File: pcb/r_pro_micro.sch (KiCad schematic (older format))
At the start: 27 parts, among them J1 Conn_01x12, J2 USB_A, J3 Conn_01x12, U1 MIC5219-2.5YM5, U2 ATmega32U4-MU, Y1 16MHz

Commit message: ** e agrega informacion de digikey en componentes importantes **
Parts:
- D1: DK# (none) -> B0520WS-FDITR-ND; MFG# (none) -> B0520WS-7-F; Manufacturer (none) -> Diodes Incorporated
- F1: DK# (none) -> 507-1762-2-ND; MFG# (none) -> 0ZCG0050AF2C; Manufacturer (none) -> Bel Fuse Inc.
- J1, J3: DK# (none) -> S1032E-12-ND; MFG# (none) -> PEC12SACN; Manufacturer (none) -> Sullins Connector Solutions
- J2: DK# (none) -> WM17143TR-ND; MFG# (none) -> 0475890001; Manufacturer (none) -> Molex
- U1: DK# (none) -> MIC5219-2.85BMM-TR-ND; MFG# (none) -> MIC5219-2.85BMM-TR; Manufacturer (none) -> Microchip Technology
- U2: DK# (none) -> ATMEGA32U4-MU-ND; MFG# (none) -> ATMEGA32U4-MU; Manufacturer (none) -> Microchip Technology
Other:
- note removed: "Digikey N producto: 507-1762-2-ND\nNumero pieza fabricante: 0ZCG0050AF2C\nDescripcion: PTC RESET FUSE 30V 500MA 1812\nProovedor: Bel Fuse Inc."
- note removed: "Digikey N producto: ATMEGA32U4-MU-ND\nDescripcion: IC MCU 8BIT 32KB FLASH 44VQFN\nProovedor: Microchip Technology"
- note removed: "Digikey N producto: B0520WS-FDITR-ND\nDescripcion: DIODE SCHOTTKY 20V 500MA SOD323\nProovedor: Diodes Incorporated"
- note removed: "Digikey N producto: MIC5219-2.85BMM-ND\nDescripcion: IC REG LINEAR 2.85V 500MA 8MSOP\nProovedor: Microchip Technology"
- note removed: "Digikey N producto: S1032E-12-ND\nDescripcion: CONN HEADER VERT 12POS 2.54MM\nProovedor: Sullins Connector Solutions"
- note removed: "Digikey N producto: WM17143TR-ND\nNumero pieza fabricante: 0475890001\nDescripcion: CONN RCPT MICRO USB AB 5P SMD RA\nProovedor: Molex"
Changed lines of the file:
@@
 F 2 "Connector_PinHeader_2.54mm:PinHeader_1x12_P2.54mm_Vertical" H 10650 3200 50  0001 C CNN
 F 3 "~" H 10650 3200 50  0001 C CNN
+F 4 "PEC12SACN" H 10650 3200 50  0001 C CNN "MFG#"
+F 5 "S1032E-12-ND" H 10650 3200 50  0001 C CNN "DK#"
+F 6 "Sullins Connector Solutions" H 10650 3200 50  0001 C CNN "Manufacturer"
 	1    10650 3200
 	1    0    0    -1
@@
 F 2 "Connector_USB:USB_Micro-AB_Molex_47590-0001" H 3200 4350 50  0001 C CNN
 F 3 " ~" H 3200 4350 50  0001 C CNN
+F 4 "0475890001" H 3050 4400 50  0001 C CNN "MFG#"
+F 5 "WM17143TR-ND" H 3050 4400 50  0001 C CNN "DK#"
+F 6 "Molex" H 3050 4400 50  0001 C CNN "Manufacturer"
 	1    3050 4400
 	1    0    0    -1
@@
 F 2 "Connector_PinHeader_2.54mm:PinHeader_1x12_P2.54mm_Vertical" H 8950 3300 50  0001 C CNN
 F 3 "~" H 8950 3300 50  0001 C CNN
+F 4 "PEC12SACN" H 8950 3300 50  0001 C CNN "MFG#"
+F 5 "S1032E-12-ND" H 8950 3300 50  0001 C CNN "DK#"
+F 6 "Sullins Connector Solutions" H 8950 3300 50  0001 C CNN "Manufacturer"
 	1    8950 3300
 	-1   0    0    1
@@
 F 2 "Package_DFN_QFN:QFN-44-1EP_7x7mm_P0.5mm_EP5.2x5.2mm" H 6400 3750 50  0001 C CIN
 F 3 "http://ww1.microchip.com/downloads/en/DeviceDoc/Atmel-7766-8-bit-AVR-ATmega16U4-32U4_Datasheet.pdf" H 6400 3750 50  0001 C CNN
+F 4 "ATMEGA32U4-MU" H 6400 3750 50  0001 C CNN "MFG#"
+F 5 "ATMEGA32U4-MU-ND" H 6400 3750 50  0001 C CNN "DK#"
+F 6 "Microchip Technology" H 6400 3750 50  0001 C CNN "Manufacturer"
 	1    6400 3750
 	1    0    0    -1
@@
 Wire Wire Line
 	5150 3350 5800 3350
-Wire Notes Line
-	6800 5450 7050 5700
-Wire Notes Line
-	7050 5700 7600 5700
-Text Notes 7050 5700 0    50   ~ 0
-Digikey N producto: ATMEGA32U4-MU-ND\nDescripcion: IC MCU 8BIT 32KB FLASH 44VQFN\nProovedor: Microchip Technology
-Text Notes 9300 4350 0    50   ~ 0
-Digikey N producto: S1032E-12-ND\nDescripcion: CONN HEADER VERT 12POS 2.54MM\nProovedor: Sullins Connector Solutions
-Wire Notes Line
-	9000 3850 9300 4100
-Wire Notes Line
-	9300 4100 9850 4100
-Wire Notes Line
-	700  1350 1350 1350
-Text Notes 2750 1650 0    50   ~ 0
-Digikey N producto: MIC5219-2.85BMM-ND\nDescripcion: IC REG LINEAR 2.85V 500MA 8MSOP\nProovedor: Microchip Technology
-Wire Notes Line
-	700  2900 1200 2900
-Wire Notes Line
-	950  1800 700  2900
-Wire Notes Line
-	2750 1650 3100 1650
-Wire Notes Line
-	2500 1900 2750 1650
 $Comp
 L Device:C_Small C6
@@
 F 2 "Diode_SMD:D_SOD-323" V 1450 1750 50  0001 C CNN
 F 3 "~" V 1450 1750 50  0001 C CNN
+F 4 "B0520WS-7-F" H 1450 1750 50  0001 C CNN "MFG#"
+F 5 "B0520WS-FDITR-ND" H 1450 1750 50  0001 C CNN "DK#"
+F 6 "Diodes Incorporated" H 1450 1750 50  0001 C CNN "Manufacturer"
 	1    1450 1750
 	-1   0    0    1
@@
 F 2 "Fuse:Fuse_1206_3216Metric" H 1050 1550 50  0001 L CNN
 F 3 "~" H 1000 1750 50  0001 C CNN
+F 4 "0ZCG0050AF2C" V 1000 1750 50  0001 C CNN "MFG#"
+F 5 "507-1762-2-ND" V 1000 1750 50  0001 C CNN "DK#"
+F 6 "Bel Fuse Inc." V 1000 1750 50  0001 C CNN "Manufacturer"
 	1    1000 1750
 	0    1    1    0
@@
 F 2 "Package_TO_SOT_SMD:SOT-23-5" H 2350 2525 50  0001 C CNN
 F 3 "http://ww1.microchip.com/downloads/en/DeviceDoc/MIC5219-500mA-Peak-Output-LDO-Regulator-DS20006021A.pdf" H 2350 2200 50  0001 C CNN
+F 4 "MIC5219-2.85BMM-TR" H 2350 2200 50  0001 C CNN "MFG#"
+F 5 "MIC5219-2.85BMM-TR-ND" H 2350 2200 50  0001 C CNN "DK#"
+F 6 "Microchip Technology" H 2350 2200 50  0001 C CNN "Manufacturer"
 	1    2350 2200
 	1    0    0    -1
 $EndComp
-Wire Notes Line
-	1400 1700 700  1350
-Text Notes 700  3250 0    50   ~ 0
-Digikey N producto: 507-1762-2-ND\nNumero pieza fabricante: 0ZCG0050AF2C\nDescripcion: PTC RESET FUSE 30V 500MA 1812\nProovedor: Bel Fuse Inc.
-Text Notes 700  1350 0    50   ~ 0
-Digikey N producto: B0520WS-FDITR-ND\nDescripcion: DIODE SCHOTTKY 20V 500MA SOD323\nProovedor: Diodes Incorporated
-Wire Notes Line
-	2850 4700 2300 5400
-Wire Notes Line
-	2300 5400 2900 5400
-Text Notes 2300 5750 0    50   ~ 0
-Digikey N producto: WM17143TR-ND\nNumero pieza fabricante: 0475890001\nDescripcion: CONN RCPT MICRO USB AB 5P SMD RA\nProovedor: Molex
 Text Label 9400 2800 0    50   ~ 0
 RXI

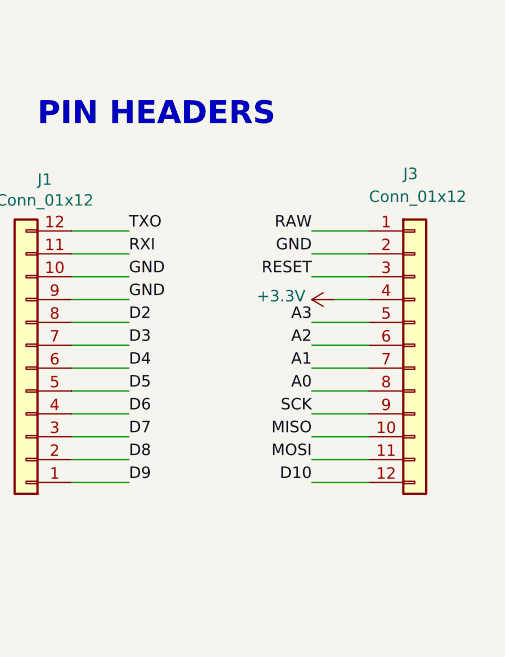
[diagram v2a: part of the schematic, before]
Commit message: ** Se rehace posicionamiento de footprints **
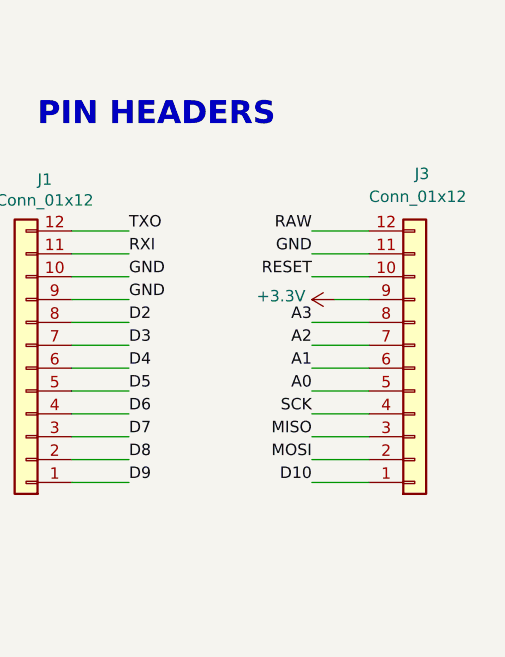
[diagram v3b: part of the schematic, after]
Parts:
- D1: footprint Diode_SMD:D_SOD-323 -> Diode_SMD:D_SOD-523
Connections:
- net +3V3: now also J3.9 (Pin_9); no longer J3.4 (Pin_4)
- net A0: now also J3.5 (Pin_5); no longer J3.8 (Pin_8)
- net A1: now also J3.6 (Pin_6); no longer J3.7 (Pin_7)
- net A2: now also J3.7 (Pin_7); no longer J3.6 (Pin_6)
- net A3: now also J3.8 (Pin_8); no longer J3.5 (Pin_5)
- net D10: now also J3.1 (Pin_1); no longer J3.12 (Pin_12)
- net GND: now also J3.11 (Pin_11); no longer J3.2 (Pin_2)
- net MISO: now also J3.3 (Pin_3); no longer J3.10 (Pin_10)
- net MOSI: now also J3.2 (Pin_2); no longer J3.11 (Pin_11)
- net RAW: now also J3.12 (Pin_12); no longer J3.1 (Pin_1)
- net RESET: now also J3.10 (Pin_10); no longer J3.3 (Pin_3)
- net SCK: now also J3.4 (Pin_4); no longer J3.9 (Pin_9)
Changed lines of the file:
@@
 L Connector_Generic:Conn_01x12 J3
 U 1 1 5F5DDF99
-P 10650 3200
-F 0 "J3" H 10600 3950 50  0000 L CNN
-F 1 "Conn_01x12" H 10450 3850 50  0000 L CNN
-F 2 "Connector_PinHeader_2.54mm:PinHeader_1x12_P2.54mm_Vertical" H 10650 3200 50  0001 C CNN
-F 3 "~" H 10650 3200 50  0001 C CNN
-F 4 "PEC12SACN" H 10650 3200 50  0001 C CNN "MFG#"
-F 5 "S1032E-12-ND" H 10650 3200 50  0001 C CNN "DK#"
-F 6 "Sullins Connector Solutions" H 10650 3200 50  0001 C CNN "Manufacturer"
-	1    10650 3200
-	1    0    0    -1
+P 10650 3300
+F 0 "J3" H 10650 2450 50  0000 L CNN
+F 1 "Conn_01x12" H 10450 2550 50  0000 L CNN
+F 2 "Connector_PinHeader_2.54mm:PinHeader_1x12_P2.54mm_Vertical" H 10650 3300 50  0001 C CNN
+F 3 "~" H 10650 3300 50  0001 C CNN
+F 4 "PEC12SACN" H 10650 3300 50  0001 C CNN "MFG#"
+F 5 "S1032E-12-ND" H 10650 3300 50  0001 C CNN "DK#"
+F 6 "Sullins Connector Solutions" H 10650 3300 50  0001 C CNN "Manufacturer"
+	1    10650 3300
+	1    0    0    1
 $EndComp
 Wire Wire Line
@@
 F 0 "D1" H 1500 1550 50  0000 C CNN
 F 1 "B0520WS-7-F" H 1300 1650 50  0000 C CNN
-F 2 "Diode_SMD:D_SOD-323" V 1450 1750 50  0001 C CNN
+F 2 "Diode_SMD:D_SOD-523" V 1450 1750 50  0001 C CNN
 F 3 "~" V 1450 1750 50  0001 C CNN
 F 4 "B0520WS-7-F" H 1450 1750 50  0001 C CNN "MFG#"

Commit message: ** Se hace completa el ruteo
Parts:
- J2: footprint Connector_USB:USB_Micro-AB_Molex_47590-0001 -> Connector_USB:USB_Micro-B_Molex_47346-0001
- Y1: footprint Crystal:Crystal_SMD_5032-4Pin_5.0x3.2mm -> Crystal:Crystal_SMD_3225-4Pin_3.2x2.5mm
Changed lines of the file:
@@
 F 0 "J2" H 3107 4867 50  0000 C CNN
 F 1 "USB_A" H 3107 4776 50  0000 C CNN
-F 2 "Connector_USB:USB_Micro-AB_Molex_47590-0001" H 3200 4350 50  0001 C CNN
+F 2 "Connector_USB:USB_Micro-B_Molex_47346-0001" H 3200 4350 50  0001 C CNN
 F 3 " ~" H 3200 4350 50  0001 C CNN
 F 4 "0475890001" H 3050 4400 50  0001 C CNN "MFG#"
@@
 F 0 "Y1" H 4750 2550 50  0000 L CNN
 F 1 "16MHz" H 4700 2750 50  0000 L CNN
-F 2 "Crystal:Crystal_SMD_5032-4Pin_5.0x3.2mm" H 4800 2650 50  0001 C CNN
+F 2 "Crystal:Crystal_SMD_3225-4Pin_3.2x2.5mm" H 4800 2650 50  0001 C CNN
 F 3 "~" H 4800 2650 50  0001 C CNN
 	1    4800 2650

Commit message: Se reahace PCB
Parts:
- removed NT1: Net-Tie_2, NetTie:NetTie-2_SMD_Pad0.5mm, symbol Device:Net-Tie_2
- added FID1, FID2: Fiducial, Fiducial:Fiducial_0.5mm_Mask1mm, symbol Mechanical:Fiducial
- added H1, H2: MountingHole, MountingHole:MountingHole_2.1mm, symbol Mechanical:MountingHole
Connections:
- net +3V3: now also J3.4 (Pin_4); no longer J3.9 (Pin_9)
- net A0: now also J3.8 (Pin_8); no longer J3.5 (Pin_5)
- net A1: now also J3.7 (Pin_7); no longer J3.6 (Pin_6)
- net A2: now also J3.6 (Pin_6); no longer J3.7 (Pin_7)
- net A3: now also J3.5 (Pin_5); no longer J3.8 (Pin_8)
- net D10: now also J3.12 (Pin_12); no longer J3.1 (Pin_1)
- net D2: now also J1.5 (Pin_5); no longer J1.8 (Pin_8)
- net D3: now also J1.6 (Pin_6); no longer J1.7 (Pin_7)
- net D4: now also J1.7 (Pin_7); no longer J1.6 (Pin_6)
- net D5: now also J1.8 (Pin_8); no longer J1.5 (Pin_5)
- net D6: now also J1.9 (Pin_9); no longer J1.4 (Pin_4)
- net D7: now also J1.10 (Pin_10); no longer J1.3 (Pin_3)
- net D8: now also J1.11 (Pin_11); no longer J1.2 (Pin_2)
- net D9: now also J1.12 (Pin_12); no longer J1.1 (Pin_1)
- net GND: now also J1.3 (Pin_3), J1.4 (Pin_4), J3.2 (Pin_2), U2.33 (~HWB~/PE2); no longer J1.10 (Pin_10), J1.9 (Pin_9), J3.11 (Pin_11)
- net MISO: now also J3.10 (Pin_10); no longer J3.3 (Pin_3)
- net MOSI: now also J3.11 (Pin_11); no longer J3.2 (Pin_2)
- net RAW: now also J3.1 (Pin_1); no longer J3.12 (Pin_12)
- net RESET: now also J3.3 (Pin_3); no longer J3.10 (Pin_10)
- net RXI: now also J1.2 (Pin_2); no longer J1.11 (Pin_11)
- net SCK: now also J3.9 (Pin_9); no longer J3.4 (Pin_4)
- net TXO: now also J1.1 (Pin_1); no longer J1.12 (Pin_12)
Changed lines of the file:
@@
 L Connector_Generic:Conn_01x12 J3
 U 1 1 5F5DDF99
-P 10650 3300
-F 0 "J3" H 10650 2450 50  0000 L CNN
-F 1 "Conn_01x12" H 10450 2550 50  0000 L CNN
-F 2 "Connector_PinHeader_2.54mm:PinHeader_1x12_P2.54mm_Vertical" H 10650 3300 50  0001 C CNN
-F 3 "~" H 10650 3300 50  0001 C CNN
-F 4 "PEC12SACN" H 10650 3300 50  0001 C CNN "MFG#"
-F 5 "S1032E-12-ND" H 10650 3300 50  0001 C CNN "DK#"
-F 6 "Sullins Connector Solutions" H 10650 3300 50  0001 C CNN "Manufacturer"
-	1    10650 3300
-	1    0    0    1
+P 10650 3200
+F 0 "J3" H 10650 2350 50  0000 L CNN
+F 1 "Conn_01x12" H 10450 2450 50  0000 L CNN
+F 2 "Connector_PinHeader_2.54mm:PinHeader_1x12_P2.54mm_Vertical" H 10650 3200 50  0001 C CNN
+F 3 "~" H 10650 3200 50  0001 C CNN
+F 4 "PEC12SACN" H 10650 3200 50  0001 C CNN "MFG#"
+F 5 "S1032E-12-ND" H 10650 3200 50  0001 C CNN "DK#"
+F 6 "Sullins Connector Solutions" H 10650 3200 50  0001 C CNN "Manufacturer"
+	1    10650 3200
+	1    0    0    -1
 $EndComp
 Wire Wire Line
@@
 L Connector_Generic:Conn_01x12 J1
 U 1 1 5F5DF74D
-P 8950 3300
-F 0 "J1" H 8868 2475 50  0000 C CNN
-F 1 "Conn_01x12" H 8868 2566 50  0000 C CNN
-F 2 "Connector_PinHeader_2.54mm:PinHeader_1x12_P2.54mm_Vertical" H 8950 3300 50  0001 C CNN
-F 3 "~" H 8950 3300 50  0001 C CNN
-F 4 "PEC12SACN" H 8950 3300 50  0001 C CNN "MFG#"
-F 5 "S1032E-12-ND" H 8950 3300 50  0001 C CNN "DK#"
-F 6 "Sullins Connector Solutions" H 8950 3300 50  0001 C CNN "Manufacturer"
-	1    8950 3300
-	-1   0    0    1
+P 8950 3200
+F 0 "J1" H 8868 2375 50  0000 C CNN
+F 1 "Conn_01x12" H 8868 2466 50  0000 C CNN
+F 2 "Connector_PinHeader_2.54mm:PinHeader_1x12_P2.54mm_Vertical" H 8950 3200 50  0001 C CNN
+F 3 "~" H 8950 3200 50  0001 C CNN
+F 4 "PEC12SACN" H 8950 3200 50  0001 C CNN "MFG#"
+F 5 "S1032E-12-ND" H 8950 3200 50  0001 C CNN "DK#"
+F 6 "Sullins Connector Solutions" H 8950 3200 50  0001 C CNN "Manufacturer"
+	1    8950 3200
+	-1   0    0    -1
 $EndComp
 Wire Wire Line
@@
 Wire Wire Line
 	1400 4550 1400 4750
-$Comp
-L Device:Net-Tie_2 NT1
-U 1 1 5F7FD2D5
-P 7700 4350
-F 0 "NT1" H 7700 4531 50  0000 C CNN
-F 1 "Net-Tie_2" H 7700 4440 50  0000 C CNN
-F 2 "NetTie:NetTie-2_SMD_Pad0.5mm" H 7700 4350 50  0001 C CNN
-F 3 "~" H 7700 4350 50  0001 C CNN
-	1    7700 4350
-	1    0    0    -1
-$EndComp
 Wire Wire Line
 	7900 4350 7900 4700
-Wire Wire Line
-	7800 4350 7900 4350
-Wire Wire Line
-	7600 4350 7000 4350
 Wire Wire Line
 	4550 2450 5800 2450
@@
 Text Label 1500 2100 2    50   ~ 0
 RAW
+Wire Wire Line
+	7000 4350 7900 4350
+$Comp
+L Mechanical:MountingHole H1
+U 1 1 5F9C0CA1
+P 2400 6300
+F 0 "H1" H 2500 6346 50  0000 L CNN
+F 1 "MountingHole" H 2500 6255 50  0000 L CNN
+F 2 "MountingHole:MountingHole_2.1mm" H 2400 6300 50  0001 C CNN
+F 3 "~" H 2400 6300 50  0001 C CNN
+	1    2400 6300
+	1    0    0    -1
+$EndComp
+$Comp
+L Mechanical:MountingHole H2
+U 1 1 5F9C10CF
+P 2400 6700
+F 0 "H2" H 2500 6746 50  0000 L CNN
+F 1 "MountingHole" H 2500 6655 50  0000 L CNN
+F 2 "MountingHole:MountingHole_2.1mm" H 2400 6700 50  0001 C CNN
+F 3 "~" H 2400 6700 50  0001 C CNN
+	1    2400 6700
+	1    0    0    -1
+$EndComp
+$Comp
+L Mechanical:Fiducial FID1
+U 1 1 5F9C5B25
+P 1000 6300
+F 0 "FID1" H 1085 6346 50  0000 L CNN
+F 1 "Fiducial" H 1085 6255 50  0000 L CNN
+F 2 "Fiducial:Fiducial_0.5mm_Mask1mm" H 1000 6300 50  0001 C CNN
+F 3 "~" H 1000 6300 50  0001 C CNN
+	1    1000 6300
+	1    0    0    -1
+$EndComp
+$Comp
+L Mechanical:Fiducial FID2
+U 1 1 5F9C5D07
+P 1000 6700
+F 0 "FID2" H 1085 6746 50  0000 L CNN
+F 1 "Fiducial" H 1085 6655 50  0000 L CNN
+F 2 "Fiducial:Fiducial_0.5mm_Mask1mm" H 1000 6700 50  0001 C CNN
+F 3 "~" H 1000 6700 50  0001 C CNN
+	1    1000 6700
+	1    0    0    -1
+$EndComp
 $EndSCHEMATC
